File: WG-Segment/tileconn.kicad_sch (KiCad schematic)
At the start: 28 parts, among them J10 Conn_01x02, J11 Conn_01x02, J12 Conn_01x02, J13 Conn_01x02, J14 Conn_01x02, J15 Conn_01x02, J16 Conn_01x02, J17 Conn_01x02, J18 Conn_01x02, J19 Conn_01x02, J2 Conn_01x02, J20 Conn_01x02, J21 Conn_01x02, J22 Conn_01x02, J23 Conn_01x02, J24 Conn_01x02, J25 Conn_01x02, J26 Conn_01x02, J3 Conn_01x02, J4 Conn_01x02, J5 Conn_01x02, J6 Conn_01x02, J7 Conn_01x02, J8 Conn_01x02, J9 Conn_01x02, U1 CD74HC4067SM, U2 CD74HC4067SM

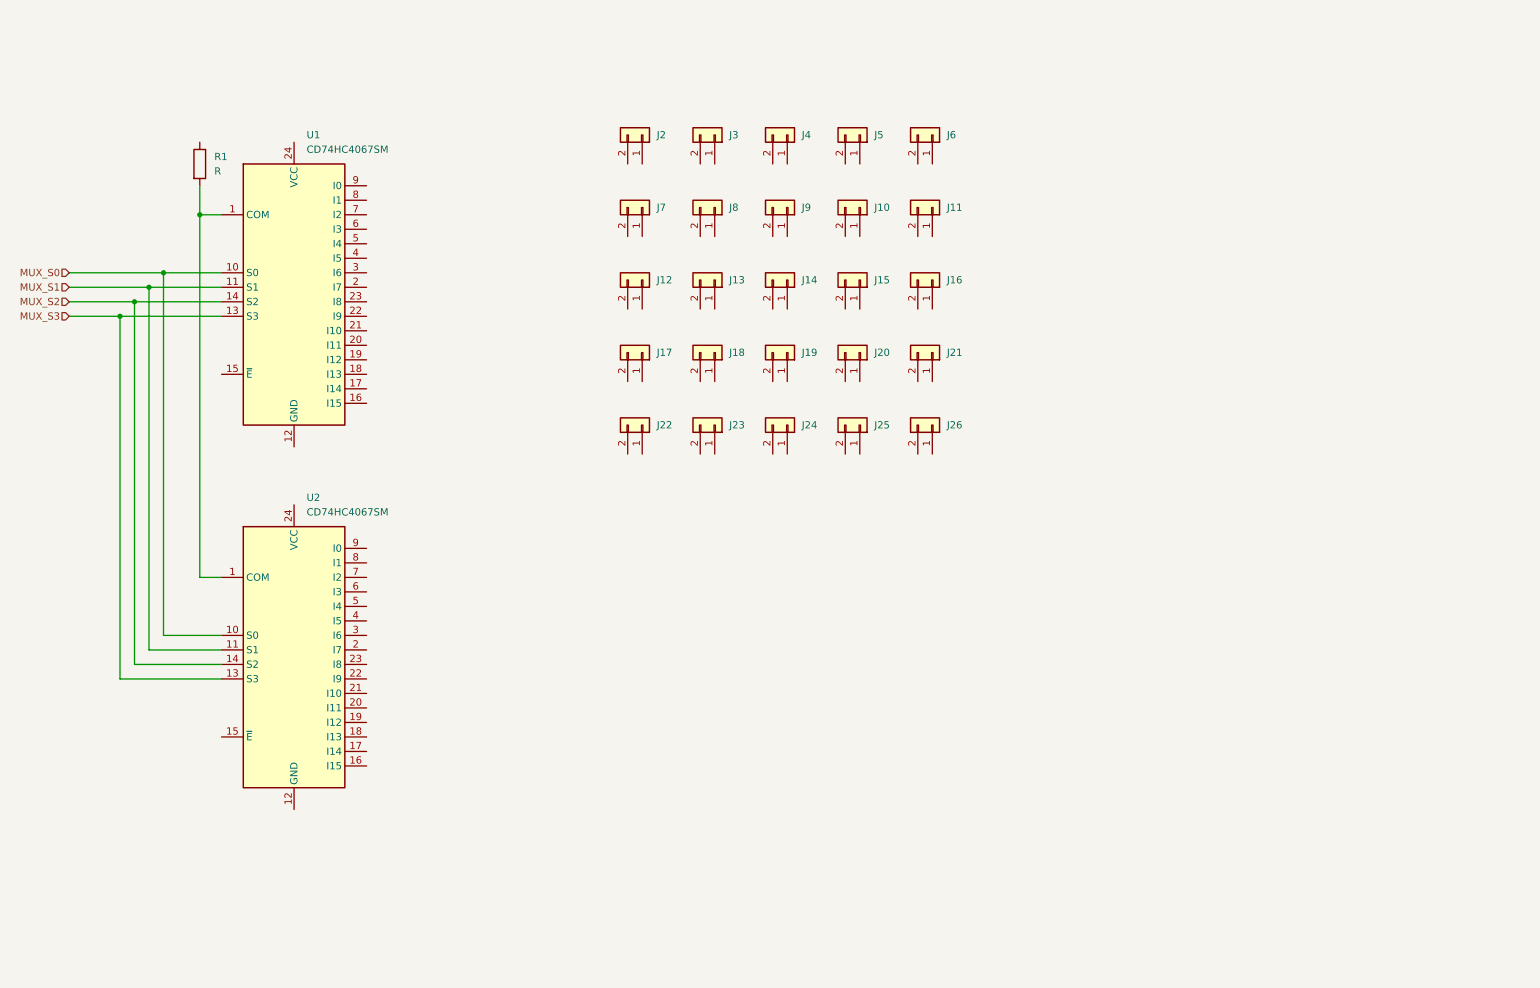
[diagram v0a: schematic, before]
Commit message: Design full circuit
Still need to run ERC
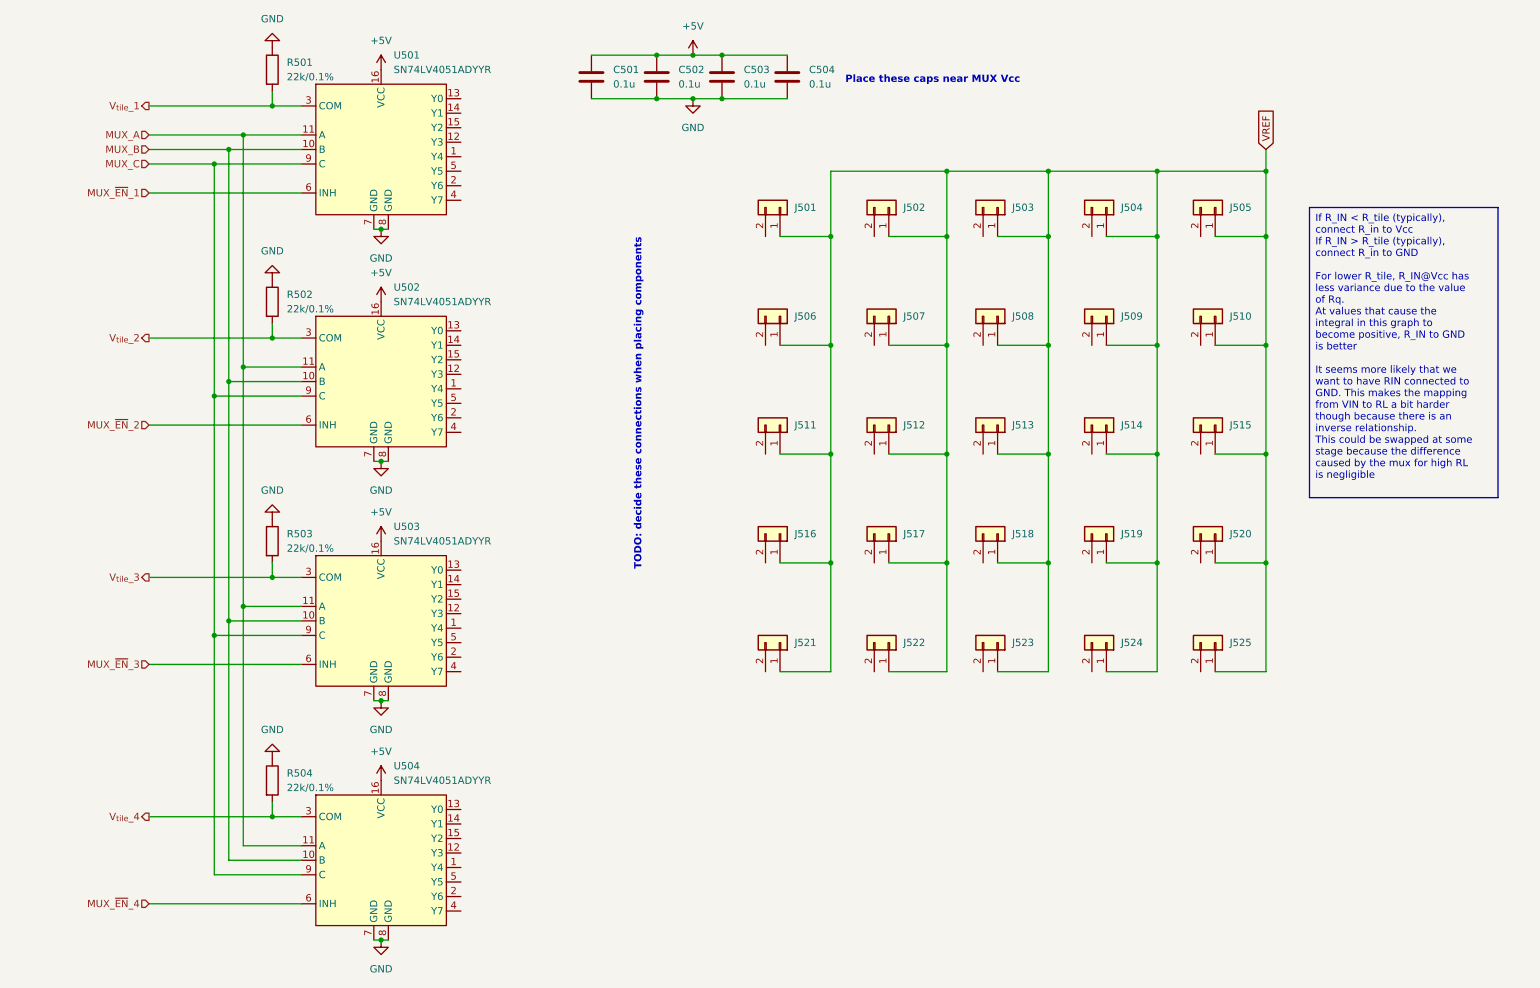
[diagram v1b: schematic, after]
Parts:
- removed R1: R, symbol Device:R
- removed U1, U2: CD74HC4067SM, Package_SO:SSOP-24_5.3x8.2mm_P0.65mm, symbol 74xx:CD74HC4067SM
- added C501, C502, C503, C504: 0.1u, Capacitor_SMD:C_0402_1005Metric_Pad0.74x0.62mm_HandSolder, symbol Device:C
- added R501, R502, R503, R504: 22k/0.1%, Resistor_SMD:R_0402_1005Metric_Pad0.72x0.64mm_HandSolder, symbol Device:R
- added U501, U502, U503, U504: SN74LV4051ADYYR, WordGameLib:SOT-23-THIN-16, symbol WordGameLib:SN74LV4051A
- renumbered J2 to J501, J3 to J502, J4 to J503, J5 to J504, J6 to J505, J7 to J506, J8 to J507, J9 to J508, J10 to J509, J11 to J510, J12 to J511, J13 to J512, J14 to J513, J15 to J514, J16 to J515, J17 to J516, J18 to J517, J19 to J518, J20 to J519, J21 to J520, J22 to J521, J23 to J522, J24 to J523, J25 to J524, J26 to J525
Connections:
- net VREF: now reaches J506.1 (Pin_1)
- net VREF: now also J501.1 (Pin_1), J502.1 (Pin_1), J503.1 (Pin_1), J504.1 (Pin_1), J505.1 (Pin_1), J507.1 (Pin_1), J508.1 (Pin_1), J509.1 (Pin_1), J510.1 (Pin_1), J511.1 (Pin_1), J512.1 (Pin_1), J513.1 (Pin_1), J514.1 (Pin_1), J515.1 (Pin_1), J516.1 (Pin_1), J517.1 (Pin_1), J518.1 (Pin_1), J519.1 (Pin_1), J520.1 (Pin_1), J521.1 (Pin_1), J522.1 (Pin_1), J523.1 (Pin_1), J524.1 (Pin_1), J525.1 (Pin_1)
- new net +5V: C501.1, C502.1, C503.1, C504.1, U501.16 (VCC), U502.16 (VCC), U503.16 (VCC), U504.16 (VCC)
- new net GND: C501.2, C502.2, C503.2, C504.2, R501.1, R502.1, R503.1, R504.1, U501.7 (GND), U501.8 (GND), U502.7 (GND), U502.8 (GND), U503.7 (GND), U503.8 (GND), U504.7 (GND), U504.8 (GND)
- new net MUX_A: U501.11 (A), U502.11 (A), U503.11 (A), U504.11 (A)
- new net MUX_B: U501.10 (B), U502.10 (B), U503.10 (B), U504.10 (B)
- new net MUX_C: U501.9 (C), U502.9 (C), U503.9 (C), U504.9 (C)
- new net MUX_~{EN}_1: U501.6 (INH)
- new net MUX_~{EN}_2: U502.6 (INH)
- new net MUX_~{EN}_3: U503.6 (INH)
- new net MUX_~{EN}_4: U504.6 (INH)
- new net V_{tile}_1: R501.2, U501.3 (COM)
- new net V_{tile}_2: R502.2, U502.3 (COM)
- new net V_{tile}_3: R503.2, U503.3 (COM)
- new net V_{tile}_4: R504.2, U504.3 (COM)
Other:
- note added: "Place these caps near MUX Vcc"
- note added: "TODO: decide these connections when placing components"
- moved on the sheet: J501, J502, J503, J504, J505, J506, J507, J508, J509, J510, J511, J512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

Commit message: Add ADC-tile connections
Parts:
- added C501, C502, C503, C504: 100n, Capacitor_SMD:C_0402_1005Metric_Pad0.74x0.62mm_HandSolder, symbol Device:C
- renumbered C501 to C505, C502 to C506, C503 to C507, C504 to C508
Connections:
- net GND: now also C501.2, C502.2, C503.2, C504.2
- net V_{tile}_1: now also C501.1
- net V_{tile}_2: now also C502.1
- net V_{tile}_3: now also C503.1
- net V_{tile}_4: now also C504.1
- net A6: now reaches J506.2 (Pin_2)
- net A6: now also U503.1 (Y4)
- net A25: now reaches J525.2 (Pin_2)
- net A25: now also U502.15 (Y2)
- net A9: now reaches J509.2 (Pin_2)
- net A9: now also U504.14 (Y1)
- net A24: now reaches J524.2 (Pin_2)
- net A24: now also U502.14 (Y1)
- net A8: now reaches J508.2 (Pin_2)
- net A8: now also U504.15 (Y2)
- net A2: now reaches J502.2 (Pin_2)
- net A2: now also U504.5 (Y5)
- net A4: now reaches J504.2 (Pin_2)
- net A4: now also U503.4 (Y7)
- net A5: now reaches J505.2 (Pin_2)
- net A5: now also U503.2 (Y6)
- net A14: now reaches U503.13 (Y0)
- net A14: now also J514.2 (Pin_2)
- net A15: now reaches U503.15 (Y2)
- net A15: now also J515.2 (Pin_2)
- net A7: now reaches U503.5 (Y5)
- net A7: now also J507.2 (Pin_2)
- net A1: now reaches J501.2 (Pin_2)
- net A1: now also U504.4 (Y7)
- net A10: now reaches J510.2 (Pin_2)
- net A10: now also U504.13 (Y0)
- net A18: now reaches J518.2 (Pin_2)
- net A18: now also U502.5 (Y5)
- net A22: now reaches J522.2 (Pin_2)
- net A22: now also U501.15 (Y2)
- net A17: now reaches J517.2 (Pin_2)
- net A17: now also U502.4 (Y7)
- net A3: now reaches U504.1 (Y4)
- net A3: now also J503.2 (Pin_2)
- net A16: now reaches J516.2 (Pin_2)
- net A16: now also U502.1 (Y4)
- net A11: now reaches J511.2 (Pin_2)
- net A11: now also U501.5 (Y5)
- net A13: now reaches J513.2 (Pin_2)
- net A13: now also U501.1 (Y4)
- net A23: now reaches U502.13 (Y0)
- net A23: now also J523.2 (Pin_2)
- net A19: now reaches J519.2 (Pin_2)
- net A19: now also U501.2 (Y6)
- net A20: now reaches U501.13 (Y0)
- net A20: now also J520.2 (Pin_2)
- net A21: now reaches U501.14 (Y1)
- net A21: now also J521.2 (Pin_2)
- net A12: now reaches U501.4 (Y7)
- net A12: now also J512.2 (Pin_2)
- no-connect marks 0 -> 7
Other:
- note removed: "TODO: decide these connections when placing components"

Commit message: Fix build issues
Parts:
- C501, C502, C503, C504: value 100n -> 0.1u; Desc (none) -> CAP CER 0.1uF 10V 0402
- C505, C506, C507, C508: Desc (none) -> CAP CER 0.1uF 10V 0402
- R501, R502, R503, R504: value 22k/0.1% -> 22k,0.1%; Desc (none) -> RES 22k 1/16W 0.1% 0402
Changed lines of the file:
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@@
       (effects (font (size 1.27 1.27)) (justify right))
     )
-    (property "Value" "100n" (at 55.88 153.67 0)
+    (property "Value" "0.1u" (at 55.88 153.67 0)
       (effects (font (size 1.27 1.27)) (justify right))
     )
@@
       (effects (font (size 1.27 1.27)) hide)
     )
-    (property "Description" "CAP CER 100nF 10V 0402" (at 59.69 152.4 0)
+    (property "Desc" "CAP CER 0.1uF 10V 0402" (at 59.69 152.4 0)
       (effects (font (size 1.27 1.27)) hide)
     )
@@
       (effects (font (size 1.27 1.27)) hide)
     )
-    (property "Description" "CAP CER 0.1u 10V 0402" (at 143.51 29.21 0)
+    (property "Desc" "CAP CER 0.1uF 10V 0402" (at 143.51 29.21 0)
       (effects (font (size 1.27 1.27)) hide)
     )
@@
       (effects (font (size 1.27 1.27)) (justify right))
     )
-    (property "Value" "100n" (at 55.88 29.21 0)
+    (property "Value" "0.1u" (at 55.88 29.21 0)
       (effects (font (size 1.27 1.27)) (justify right))
     )
@@
       (effects (font (size 1.27 1.27)) hide)
     )
-    (property "Description" "CAP CER 100nF 10V 0402" (at 59.69 27.94 0)
+    (property "Desc" "CAP CER 0.1uF 10V 0402" (at 59.69 27.94 0)
       (effects (font (size 1.27 1.27)) hide)
     )
@@
       (effects (font (size 1.27 1.27)) hide)
     )
-    (property "Description" "CAP CER 0.1u 10V 0402" (at 120.65 29.21 0)
+    (property "Desc" "CAP CER 0.1uF 10V 0402" (at 120.65 29.21 0)
       (effects (font (size 1.27 1.27)) hide)
     )
@@
       (effects (font (size 1.27 1.27)) hide)
     )
-    (property "Description" "CAP CER 0.1u 10V 0402" (at 154.94 29.21 0)
+    (property "Desc" "CAP CER 0.1uF 10V 0402" (at 154.94 29.21 0)
       (effects (font (size 1.27 1.27)) hide)
     )
@@
       (effects (font (size 1.27 1.27)) hide)
     )
-    (property "Description" "CAP CER 0.1u 10V 0402" (at 132.08 29.21 0)
+    (property "Desc" "CAP CER 0.1uF 10V 0402" (at 132.08 29.21 0)
       (effects (font (size 1.27 1.27)) hide)
     )
@@
       (effects (font (size 1.27 1.27)) (justify left))
     )
-    (property "Value" "22k/0.1%" (at 67.31 111.76 0)
+    (property "Value" "22k,0.1%" (at 67.31 111.76 0)
       (effects (font (size 1.27 1.27)) (justify left))
     )
@@
       (effects (font (size 1.27 1.27)) hide)
     )
-    (property "Description" "RES 22k 1/16W 0.1% 0402" (at 64.77 110.49 0)
+    (property "Desc" "RES 22k 1/16W 0.1% 0402" (at 64.77 110.49 0)
       (effects (font (size 1.27 1.27)) hide)
     )
@@
       (effects (font (size 1.27 1.27)) (justify left))
     )
-    (property "Value" "22k/0.1%" (at 67.31 153.67 0)
+    (property "Value" "22k,0.1%" (at 67.31 153.67 0)
       (effects (font (size 1.27 1.27)) (justify left))
     )
@@
       (effects (font (size 1.27 1.27)) hide)
     )
-    (property "Description" "RES 22k 1/16W 0.1% 0402" (at 64.77 152.4 0)
+    (property "Desc" "RES 22k 1/16W 0.1% 0402" (at 64.77 152.4 0)
       (effects (font (size 1.27 1.27)) hide)
     )
@@
       (effects (font (size 1.27 1.27)) (justify right))
     )
-    (property "Value" "100n" (at 55.88 111.76 0)
+    (property "Value" "0.1u" (at 55.88 111.76 0)
       (effects (font (size 1.27 1.27)) (justify right))
     )
@@
       (effects (font (size 1.27 1.27)) hide)
     )
-    (property "Description" "CAP CER 100nF 10V 0402" (at 59.69 110.49 0)
+    (property "Desc" "CAP CER 0.1uF 10V 0402" (at 59.69 110.49 0)
       (effects (font (size 1.27 1.27)) hide)
     )
@@
       (effects (font (size 1.27 1.27)) (justify left))
     )
-    (property "Value" "22k/0.1%" (at 67.31 29.21 0)
+    (property "Value" "22k,0.1%" (at 67.31 29.21 0)
       (effects (font (size 1.27 1.27)) (justify left))
     )
@@
       (effects (font (size 1.27 1.27)) hide)
     )
-    (property "Description" "RES 22k 1/16W 0.1% 0402" (at 64.77 27.94 0)
+    (property "Desc" "RES 22k 1/16W 0.1% 0402" (at 64.77 27.94 0)
       (effects (font (size 1.27 1.27)) hide)
     )
@@
       (effects (font (size 1.27 1.27)) (justify right))
     )
-    (property "Value" "100n" (at 55.88 69.85 0)
+    (property "Value" "0.1u" (at 55.88 69.85 0)
       (effects (font (size 1.27 1.27)) (justify right))
     )
@@
       (effects (font (size 1.27 1.27)) hide)
     )
-    (property "Description" "CAP CER 100nF 10V 0402" (at 59.69 68.58 0)
+    (property "Desc" "CAP CER 0.1uF 10V 0402" (at 59.69 68.58 0)
       (effects (font (size 1.27 1.27)) hide)
     )
@@
       (effects (font (size 1.27 1.27)) (justify left))
     )
-    (property "Value" "22k/0.1%" (at 67.31 69.85 0)
+    (property "Value" "22k,0.1%" (at 67.31 69.85 0)
       (effects (font (size 1.27 1.27)) (justify left))
     )
@@
       (effects (font (size 1.27 1.27)) hide)
     )
-    (property "Description" "RES 22k 1/16W 0.1% 0402" (at 64.77 68.58 0)
-      (effects (font (size 1.27 1.27)) hide)
-    )
+    (property "Desc" "RES 22k 1/16W 0.1% 0402" (at 64.77 68.58 0)
+      (effects (font (size 1.27 1.27)) hide)
+    )

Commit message: Change component value
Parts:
- R501, R502, R503, R504: value 22k,0.1% -> 22k/0.1%
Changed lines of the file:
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@@
       (effects (font (size 1.27 1.27)) (justify left))
     )
-    (property "Value" "22k,0.1%" (at 67.31 111.76 0)
+    (property "Value" "22k/0.1%" (at 67.31 111.76 0)
       (effects (font (size 1.27 1.27)) (justify left))
     )
@@
       (effects (font (size 1.27 1.27)) (justify left))
     )
-    (property "Value" "22k,0.1%" (at 67.31 153.67 0)
+    (property "Value" "22k/0.1%" (at 67.31 153.67 0)
       (effects (font (size 1.27 1.27)) (justify left))
     )
@@
       (effects (font (size 1.27 1.27)) (justify left))
     )
-    (property "Value" "22k,0.1%" (at 67.31 29.21 0)
+    (property "Value" "22k/0.1%" (at 67.31 29.21 0)
       (effects (font (size 1.27 1.27)) (justify left))
     )
@@
       (effects (font (size 1.27 1.27)) (justify left))
     )
-    (property "Value" "22k,0.1%" (at 67.31 69.85 0)
-      (effects (font (size 1.27 1.27)) (justify left))
-    )
+    (property "Value" "22k/0.1%" (at 67.31 69.85 0)
+      (effects (font (size 1.27 1.27)) (justify left))
+    )

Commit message: Update parts to ones in JLCPCB library
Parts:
- R501, R502, R503, R504: value 22k/0.1% -> 8k2/0.1%; Desc RES 22k 1/16W 0.1% 0402 -> RES 8k2 1/16W 0.1% 0402
- U501, U502, U503, U504: value SN74LV4051ADYYR -> SN74LV4051A; footprint WordGameLib:SOT-23-THIN-16 -> Package_SO:TSSOP-16_4.4x5mm_P0.65mm; Part Number SN74LV4051ADYYR -> SN74LV4051APWR
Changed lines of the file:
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@@
       (effects (font (size 1.27 1.27)) (justify left))
     )
-    (property "Value" "22k/0.1%" (at 67.31 111.76 0)
+    (property "Value" "8k2/0.1%" (at 67.31 111.76 0)
       (effects (font (size 1.27 1.27)) (justify left))
     )
@@
       (effects (font (size 1.27 1.27)) hide)
     )
-    (property "Desc" "RES 22k 1/16W 0.1% 0402" (at 64.77 110.49 0)
+    (property "Desc" "RES 8k2 1/16W 0.1% 0402" (at 64.77 110.49 0)
       (effects (font (size 1.27 1.27)) hide)
     )
@@
       (effects (font (size 1.27 1.27)) (justify left))
     )
-    (property "Value" "SN74LV4051ADYYR" (at 86.0141 110.49 0)
-      (effects (font (size 1.27 1.27)) (justify left))
-    )
-    (property "Footprint" "WordGameLib:SOT-23-THIN-16" (at 69.85 118.11 0)
+    (property "Value" "SN74LV4051A" (at 86.0141 110.49 0)
+      (effects (font (size 1.27 1.27)) (justify left))
+    )
+    (property "Footprint" "Package_SO:TSSOP-16_4.4x5mm_P0.65mm" (at 69.85 118.11 0)
       (effects (font (size 1.27 1.27)) hide)
     )
@@
       (effects (font (size 1.27 1.27)) hide)
     )
-    (property "Part Number" "SN74LV4051ADYYR" (at 83.82 105.41 0)
+    (property "Part Number" "SN74LV4051APWR" (at 83.82 105.41 0)
+      (effects (font (size 1.27 1.27)) hide)
+    )
+    (property "Desc" "" (at 83.82 105.41 0)
       (effects (font (size 1.27 1.27)) hide)
     )
@@
       (effects (font (size 1.27 1.27)) (justify left))
     )
-    (property "Value" "22k/0.1%" (at 67.31 153.67 0)
+    (property "Value" "8k2/0.1%" (at 67.31 153.67 0)
       (effects (font (size 1.27 1.27)) (justify left))
     )
@@
       (effects (font (size 1.27 1.27)) hide)
     )
-    (property "Desc" "RES 22k 1/16W 0.1% 0402" (at 64.77 152.4 0)
+    (property "Desc" "RES 8k2 1/16W 0.1% 0402" (at 64.77 152.4 0)
+      (effects (font (size 1.27 1.27)) hide)
+    )
+    (property "Part Number" "" (at 64.77 152.4 0)
+      (effects (font (size 1.27 1.27)) hide)
+    )
+    (property "Manufacturer" "" (at 64.77 152.4 0)
       (effects (font (size 1.27 1.27)) hide)
     )
@@
       (effects (font (size 1.27 1.27)) (justify left))
     )
-    (property "Value" "22k/0.1%" (at 67.31 29.21 0)
+    (property "Value" "8k2/0.1%" (at 67.31 29.21 0)
       (effects (font (size 1.27 1.27)) (justify left))
     )
@@
       (effects (font (size 1.27 1.27)) hide)
     )
-    (property "Desc" "RES 22k 1/16W 0.1% 0402" (at 64.77 27.94 0)
+    (property "Desc" "RES 8k2 1/16W 0.1% 0402" (at 64.77 27.94 0)
       (effects (font (size 1.27 1.27)) hide)
     )
@@
       (effects (font (size 1.27 1.27)) (justify left))
     )
-    (property "Value" "SN74LV4051ADYYR" (at 86.0141 152.4 0)
-      (effects (font (size 1.27 1.27)) (justify left))
-    )
-    (property "Footprint" "WordGameLib:SOT-23-THIN-16" (at 69.85 160.02 0)
+    (property "Value" "SN74LV4051A" (at 86.0141 152.4 0)
+      (effects (font (size 1.27 1.27)) (justify left))
+    )
+    (property "Footprint" "Package_SO:TSSOP-16_4.4x5mm_P0.65mm" (at 69.85 160.02 0)
       (effects (font (size 1.27 1.27)) hide)
     )
@@
       (effects (font (size 1.27 1.27)) hide)
     )
-    (property "Part Number" "SN74LV4051ADYYR" (at 83.82 147.32 0)
+    (property "Part Number" "SN74LV4051APWR" (at 83.82 147.32 0)
+      (effects (font (size 1.27 1.27)) hide)
+    )
+    (property "Desc" "" (at 83.82 147.32 0)
       (effects (font (size 1.27 1.27)) hide)
     )
@@
       (effects (font (size 1.27 1.27)) (justify left))
     )
-    (property "Value" "SN74LV4051ADYYR" (at 86.0141 68.58 0)
-      (effects (font (size 1.27 1.27)) (justify left))
-    )
-    (property "Footprint" "WordGameLib:SOT-23-THIN-16" (at 69.85 76.2 0)
+    (property "Value" "SN74LV4051A" (at 86.0141 68.58 0)
+      (effects (font (size 1.27 1.27)) (justify left))
+    )
+    (property "Footprint" "Package_SO:TSSOP-16_4.4x5mm_P0.65mm" (at 69.85 76.2 0)
       (effects (font (size 1.27 1.27)) hide)
     )
@@
       (effects (font (size 1.27 1.27)) hide)
     )
-    (property "Part Number" "SN74LV4051ADYYR" (at 83.82 63.5 0)
+    (property "Part Number" "SN74LV4051APWR" (at 83.82 63.5 0)
+      (effects (font (size 1.27 1.27)) hide)
+    )
+    (property "Desc" "" (at 83.82 63.5 0)
       (effects (font (size 1.27 1.27)) hide)
     )
@@
       (effects (font (size 1.27 1.27)) (justify left))
     )
-    (property "Value" "22k/0.1%" (at 67.31 69.85 0)
+    (property "Value" "8k2/0.1%" (at 67.31 69.85 0)
       (effects (font (size 1.27 1.27)) (justify left))
     )
@@
       (effects (font (size 1.27 1.27)) hide)
     )
-    (property "Desc" "RES 22k 1/16W 0.1% 0402" (at 64.77 68.58 0)
+    (property "Desc" "RES 8k2 1/16W 0.1% 0402" (at 64.77 68.58 0)
       (effects (font (size 1.27 1.27)) hide)
     )
@@
       (effects (font (size 1.27 1.27)) (justify left))
     )
-    (property "Value" "SN74LV4051ADYYR" (at 86.0141 27.94 0)
-      (effects (font (size 1.27 1.27)) (justify left))
-    )
-    (property "Footprint" "WordGameLib:SOT-23-THIN-16" (at 69.85 35.56 0)
+    (property "Value" "SN74LV4051A" (at 86.0141 27.94 0)
+      (effects (font (size 1.27 1.27)) (justify left))
+    )
+    (property "Footprint" "Package_SO:TSSOP-16_4.4x5mm_P0.65mm" (at 69.85 35.56 0)
       (effects (font (size 1.27 1.27)) hide)
     )
@@
       (effects (font (size 1.27 1.27)) hide)
     )
-    (property "Part Number" "SN74LV4051ADYYR" (at 83.82 22.86 0)
-      (effects (font (size 1.27 1.27)) hide)
-    )
+    (property "Part Number" "SN74LV4051APWR" (at 83.82 22.86 0)
+      (effects (font (size 1.27 1.27)) hide)
+    )
+    (property "Desc" "" (at 83.82 22.86 0)
+      (effects (font (size 1.27 1.27)) hide)
+    )
